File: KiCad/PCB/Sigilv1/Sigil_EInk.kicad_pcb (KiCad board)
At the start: 2 copper layers, 46 x 76 mm, 17 parts, among them J2 INLAND E-PAPER HEADER (8-PIN), J3 BUZZER 2-PIN HEADER, J4 ANALOG JOYSTICK HEADER (5-PIN), J5 STATUS RING CABLE (JST-XH 3), J6 FRONT LIGHT CABLE (JST-XH 3), U1 REMOVABLE ESP32 DEVKIT / 2 x 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, U2 74AHCT1G125, U3 74AHCT1G125

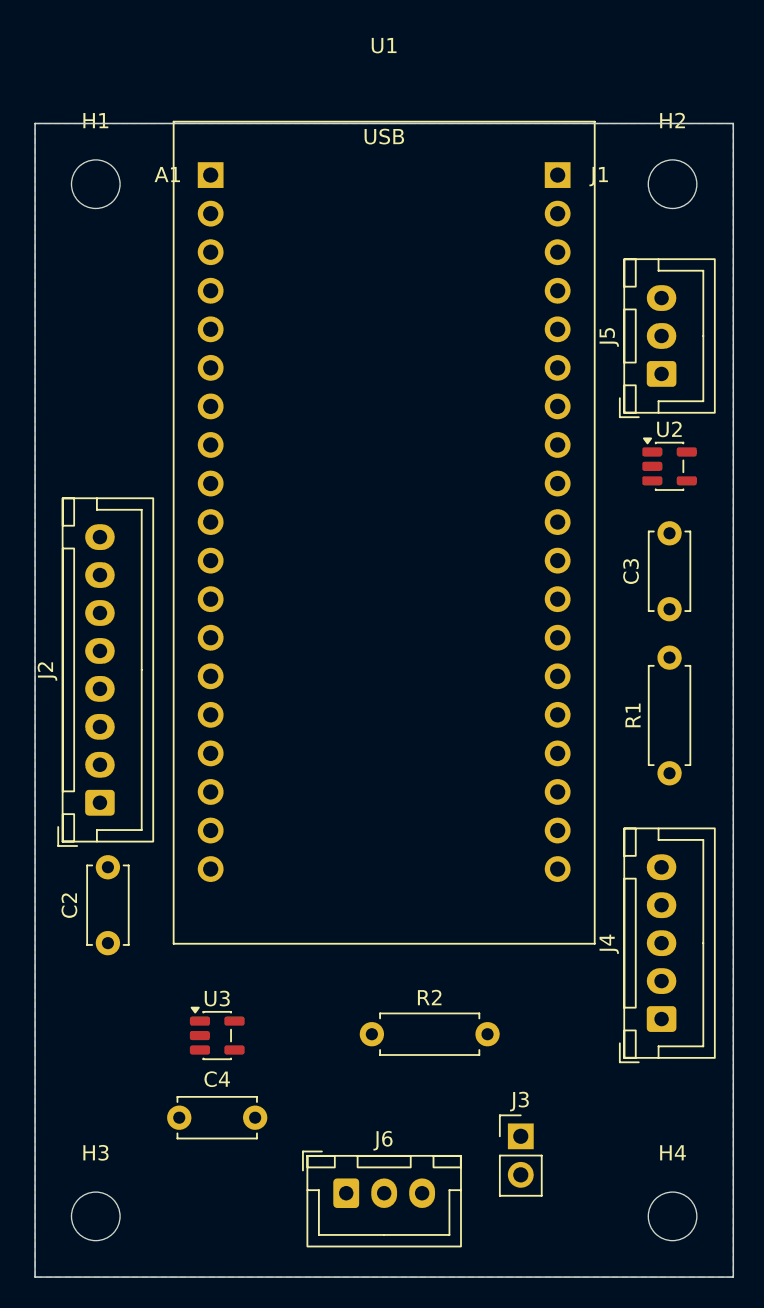
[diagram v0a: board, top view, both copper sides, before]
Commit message: Sigil E-ink PCB: measured DevKit footprint, routed board, fab outputs
- U1 footprint rows 22.225 mm (7/8 in) apart per owner measurement,
  25.4 x 53.975 mm outline; renamed ESP32_DevKit_38_Socket_Row22.225mm.
- Antenna keep-out narrowed to the measured antenna (6.35 x 19.05 mm)
  so the pin rows stay routable.
- Board top edge moved up 0.5 mm to clear silkscreen.
- Routed with Freerouting v2.4.1 plus a hand-placed BUZZER track; GND
  pours on both layers with solid pad connections. KiCad 10.0.6 DRC:
  0 violations, 0 unconnected, 0 schematic parity issues.
- Added BOM CSV, Gerber/drill zip and position CSV under fab/.
- Not fabrication-verified: U1 row spacing still needs a test-fit.

Co-Authored-By: Claude Opus 5.5 <noreply@anthropic.com>
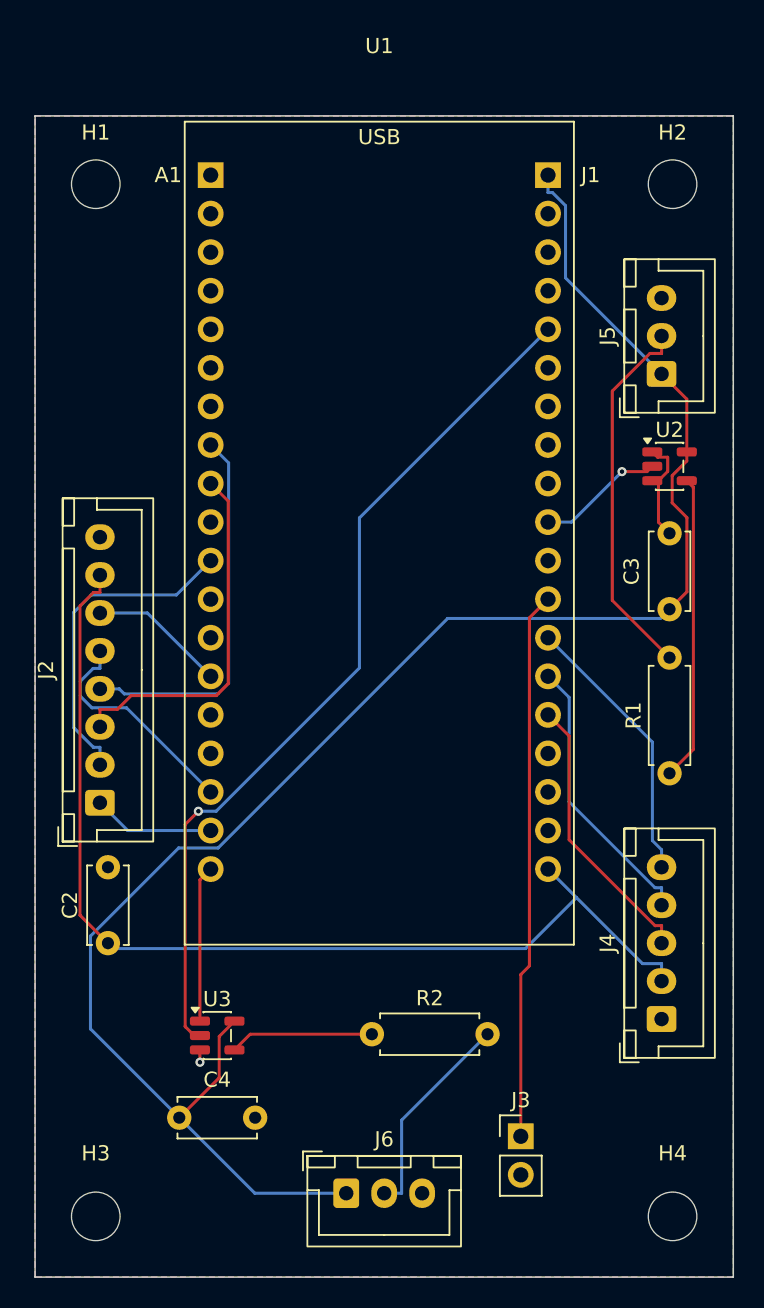
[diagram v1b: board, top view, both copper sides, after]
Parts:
- U1: footprint Sigil:ESP32_DevKit_38_Socket_Row22.86mm -> Sigil:ESP32_DevKit_38_Socket_Row22.225mm
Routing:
- net /+5V: track 0.00 -> 116.2 mm
- net /+3V3: track 0.00 -> 69.4 mm
- net /FRONT_DIN: track 0.00 -> 57.7 mm, vias 0 -> 1
- net /BUZZER: track 0.00 -> 36.1 mm
- net /EPD_DC: track 0.00 -> 25.1 mm
- net /RING_DIN_R: track 0.00 -> 24.5 mm
- net /EPD_CS: track 0.00 -> 24.0 mm
- net /EPD_SCLK: track 0.00 -> 21.4 mm
- net /RING_DIN_5V: track 0.00 -> 20.1 mm
- net /JOY_Y: track 0.00 -> 18.4 mm
- net /JOY_X: track 0.00 -> 18.4 mm
- net /GND: track 0.00 -> 18.3 mm, vias 0 -> 1
- net /JOY_SW: track 0.00 -> 18.2 mm
- net /EPD_RST: track 0.00 -> 15.0 mm
- net /FRONT_DIN_R: track 0.00 -> 14.0 mm
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- added copper zone on F.Cu, net /GND
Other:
- board size 46 x 76 mm -> 46 x 76.5 mm
